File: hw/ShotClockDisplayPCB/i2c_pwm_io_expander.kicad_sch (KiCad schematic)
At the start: 0 parts

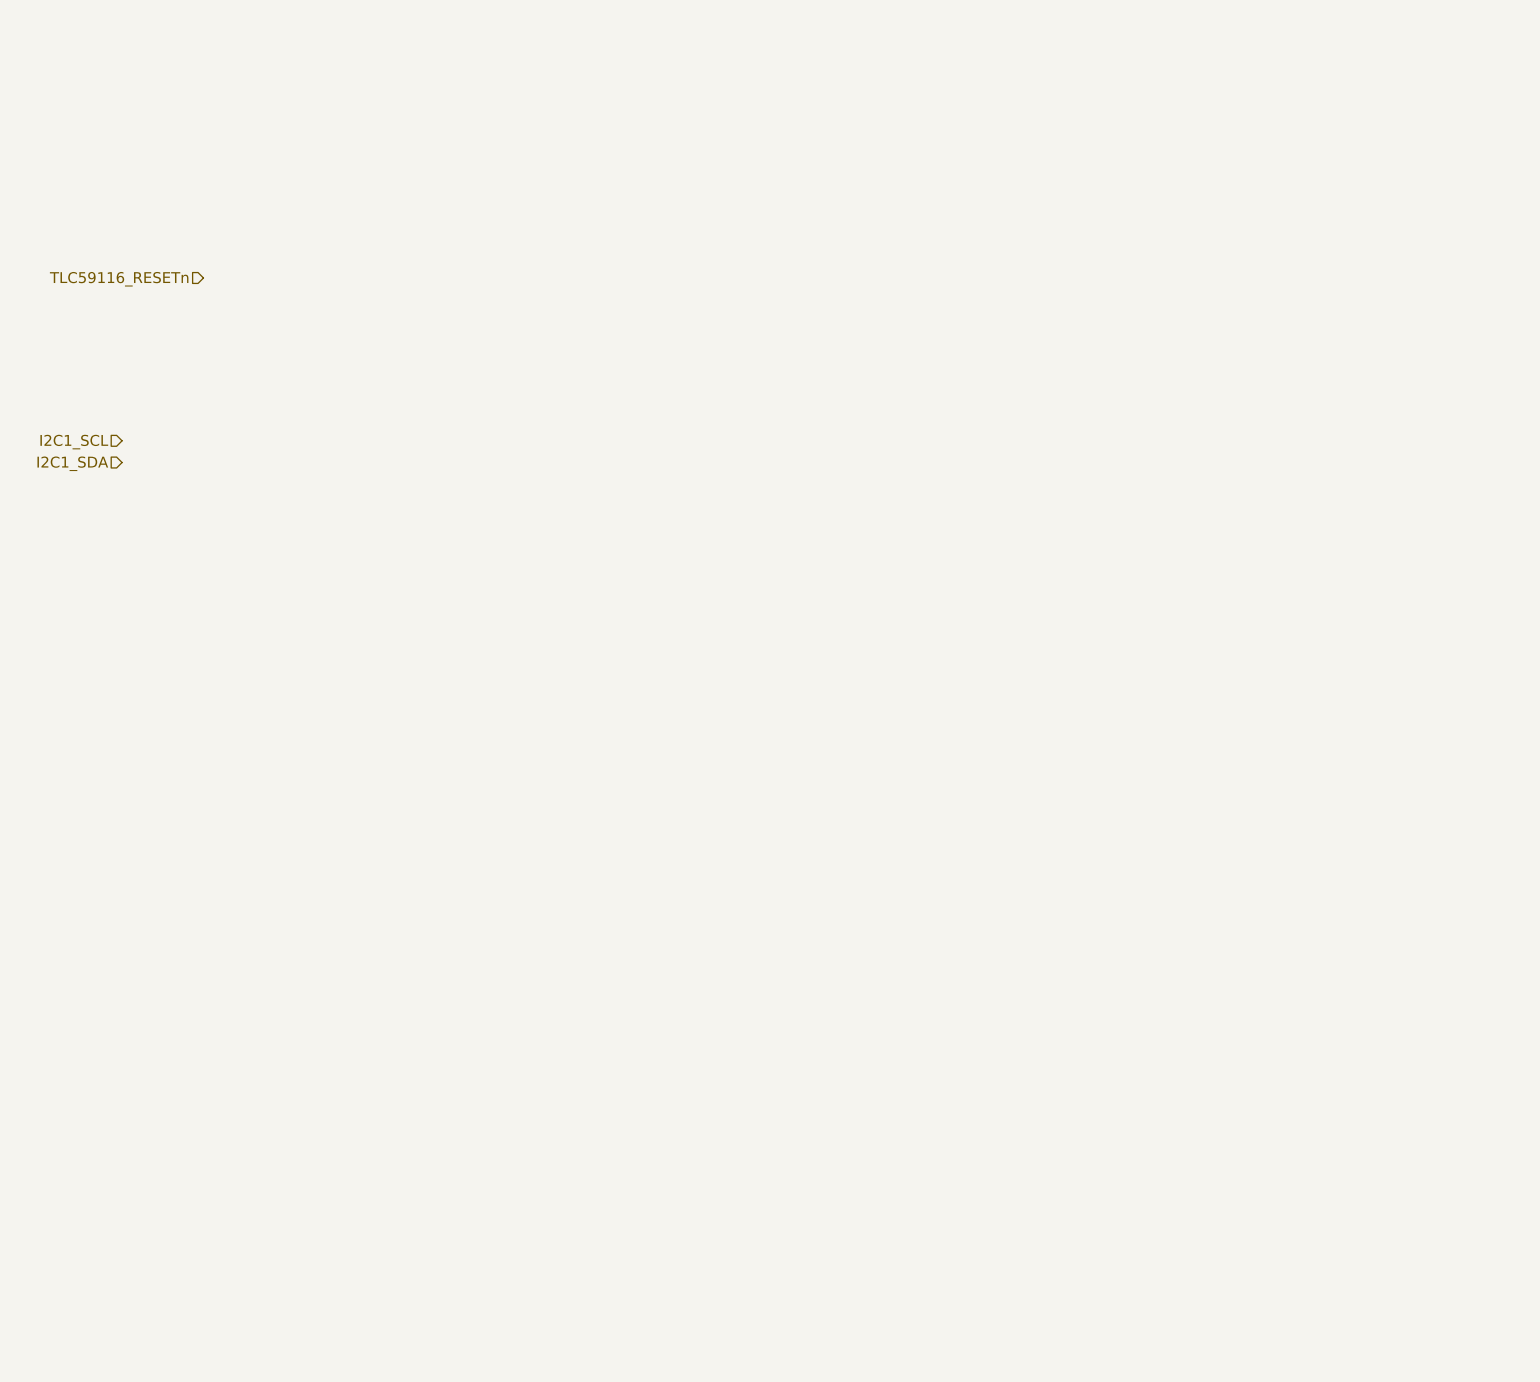
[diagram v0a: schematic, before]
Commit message: Started on display board rework
added new footprints
added HW select shunts/jumpers
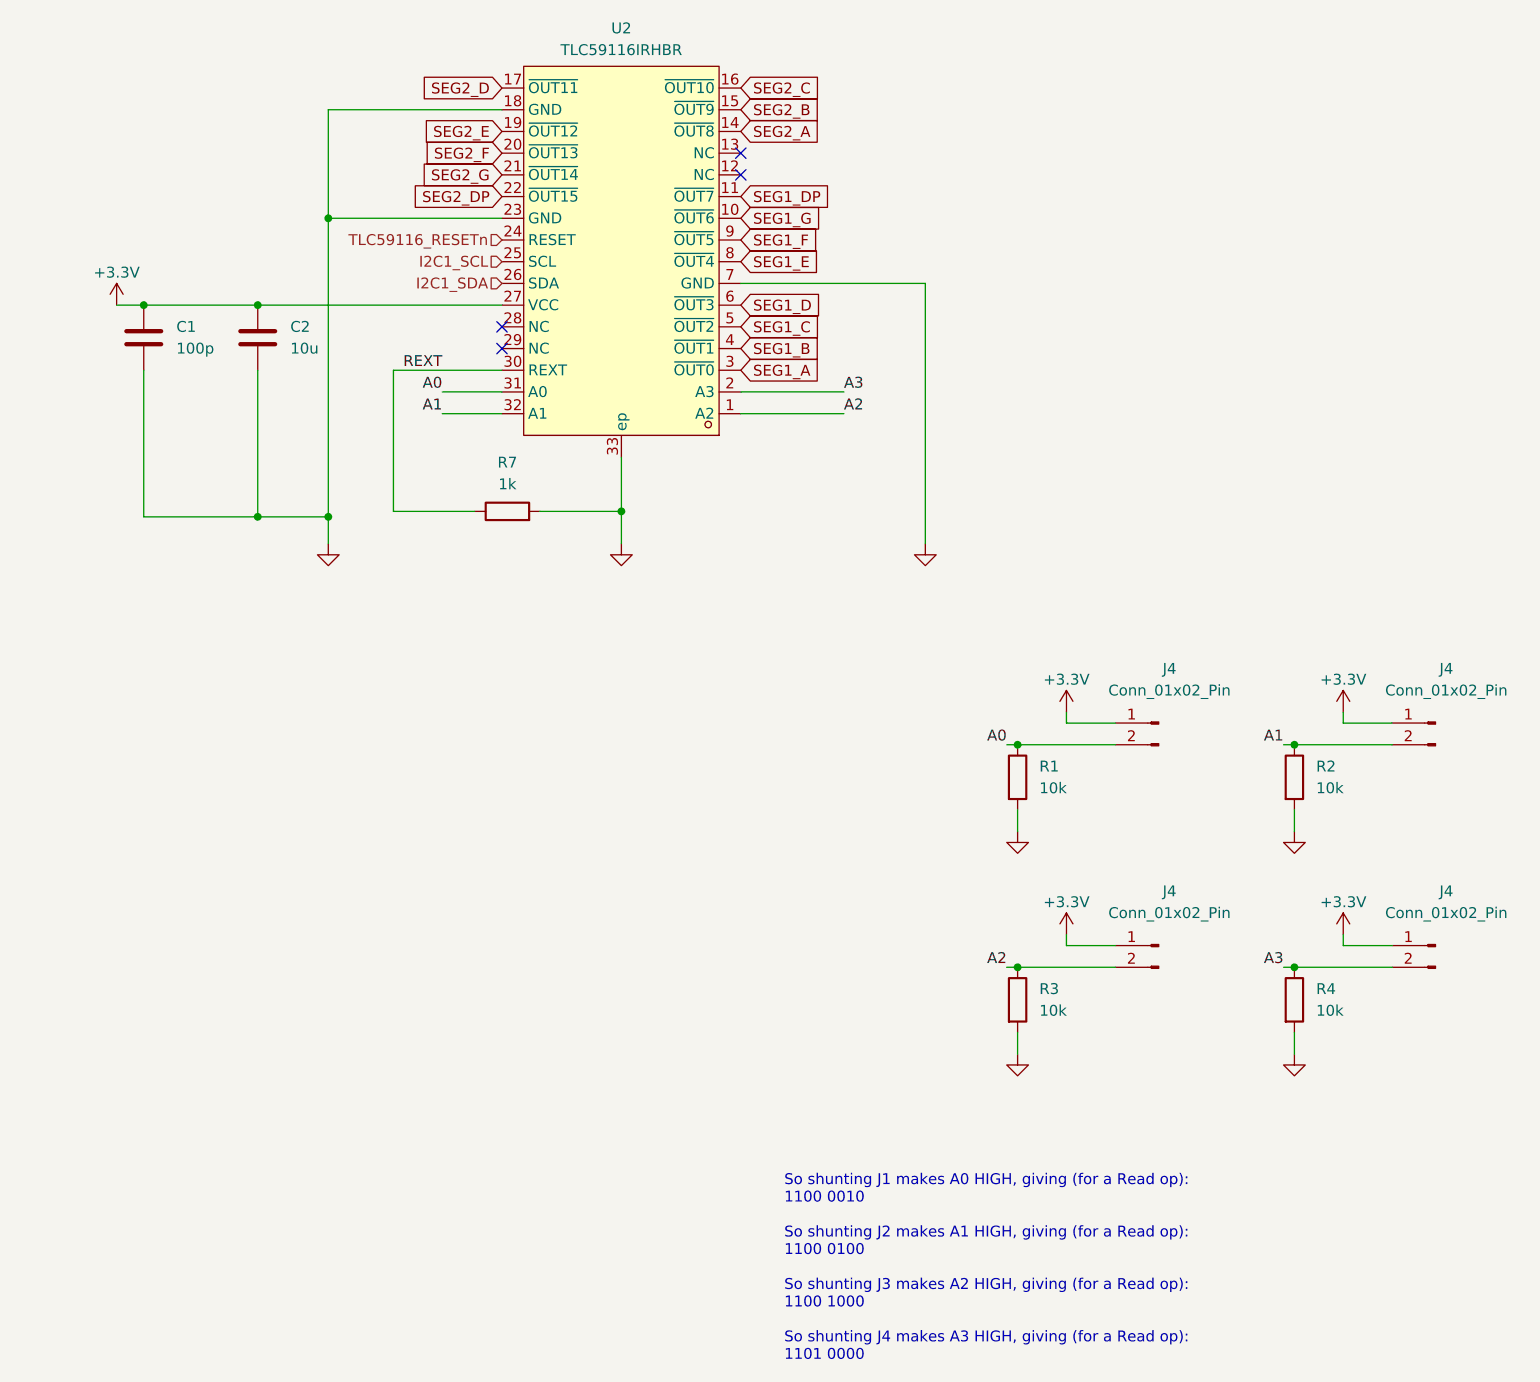
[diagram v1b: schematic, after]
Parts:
- added C1: 100p, Capacitor_SMD:C_0402_1005Metric, symbol Device:C
- added C2: 10u, Capacitor_SMD:C_0402_1005Metric, symbol Device:C
- added J4 (x4): Conn_01x02_Pin, Connector_PinHeader_2.54mm:PinHeader_1x02_P2.54mm_Horizontal, symbol Connector:Conn_01x02_Pin
- added R1, R2, R3, R4: 10k, Resistor_SMD:R_0402_1005Metric, symbol Device:R
- added R7: 1k, Resistor_SMD:R_0402_1005Metric, symbol Device:R
- added U2: TLC59116IRHBR, TLC59116IRHBR:PG-VQFN-32_L5.0-W5.0-P0.50-BL-EP3.6, symbol TLC59116IRHBR:TLC59116IRHBR
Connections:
- net I2C1_SCL: now also U2.25 (SCL)
- net I2C1_SDA: now also U2.26 (SDA)
- net TLC59116_RESETn: now also U2.24 (RESET)
- new net +3.3V: C1.1, C2.1, J4.1 (Pin_1), J4.1 (Pin_1), J4.1 (Pin_1), J4.1 (Pin_1), U2.27 (VCC)
- new net A0: J4.2 (Pin_2), R1.1, U2.31 (A0)
- new net A1: J4.2 (Pin_2), R2.1, U2.32 (A1)
- new net A2: J4.2 (Pin_2), R3.1, U2.1 (A2)
- new net A3: J4.2 (Pin_2), R4.1, U2.2 (A3)
- new net GND: C1.2, C2.2, R1.2, R2.2, R3.2, R4.2, R7.2, U2.18 (GND), U2.23 (GND), U2.33 (ep), U2.7 (GND)
- new net REXT: R7.1, U2.30 (REXT)
- new net SEG1_A: U2.3 (~{OUT0})
- new net SEG1_B: U2.4 (~{OUT1})
- new net SEG1_C: U2.5 (~{OUT2})
- new net SEG1_D: U2.6 (~{OUT3})
- new net SEG1_DP: U2.11 (~{OUT7})
- new net SEG1_E: U2.8 (~{OUT4})
- new net SEG1_F: U2.9 (~{OUT5})
- new net SEG1_G: U2.10 (~{OUT6})
- new net SEG2_A: U2.14 (~{OUT8})
- new net SEG2_B: U2.15 (~{OUT9})
- new net SEG2_C: U2.16 (~{OUT10})
- new net SEG2_D: U2.17 (~{OUT11})
- new net SEG2_DP: U2.22 (~{OUT15})
- new net SEG2_E: U2.19 (~{OUT12})
- new net SEG2_F: U2.20 (~{OUT13})
- new net SEG2_G: U2.21 (~{OUT14})
- no-connect marks 0 -> 4
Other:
- note added: "So shunting J1 makes A0 HIGH, giving (for a Read op): 1100 0010 So shunting J2 makes A1 HIGH, giving (for a Read op): 1100 0100 So shunting J3 makes A2 HIGH, giving (for a Read op): 1100 1000 So shunting J4 makes A3 HIGH, giving (for a Read op): 1101 0000"

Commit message: Changed LCSC Part numbers for disp board
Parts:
- C1: LCSC Part (none) -> C106200
- C2: LCSC Part (none) -> C315248
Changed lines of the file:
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@@
+      (effects (font (size 1.27 1.27)) hide)
+    )
+    (property "LCSC Part" "C315248" (at 47.625 64.135 0)
       (effects (font (size 1.27 1.27)) hide)
     )
@@
       (effects (font (size 1.27 1.27)) hide)
     )
+    (property "LCSC Part" "C106200" (at 34.29 64.135 0)
+      (effects (font (size 1.27 1.27)) hide)
+    )

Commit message: REV2 Finished
Corrected LCSC part number
Added polarities on silkscreen
Made output files for both boards
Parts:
- J4: LCSC Part C225269 -> C492410
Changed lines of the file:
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@@
       (effects (font (size 1.27 1.27)) hide)
     )
-    (property "LCSC Part #" "" (at 185.42 109.22 0)
-      (effects (font (size 1.27 1.27)) hide)
-    )
-    (property "LCSC Part" "C225269" (at 185.42 109.22 0)
+    (property "LCSC Part" "C492410" (at 185.42 109.22 0)
       (effects (font (size 1.27 1.27)) hide)
     )
@@
       (effects (font (size 1.27 1.27)) hide)
     )
-    (property "LCSC Part #" "" (at 185.42 135.255 0)
-      (effects (font (size 1.27 1.27)) hide)
-    )
-    (property "LCSC Part" "C225269" (at 185.42 135.255 0)
+    (property "LCSC Part" "C492410" (at 185.42 135.255 0)
       (effects (font (size 1.27 1.27)) hide)
     )
@@
       (effects (font (size 1.27 1.27)) hide)
     )
-    (property "LCSC Part #" "" (at 153.035 109.22 0)
-      (effects (font (size 1.27 1.27)) hide)
-    )
-    (property "LCSC Part" "C225269" (at 153.035 109.22 0)
+    (property "LCSC Part" "C492410" (at 153.035 109.22 0)
       (effects (font (size 1.27 1.27)) hide)
     )
@@
       (effects (font (size 1.27 1.27)) hide)
     )
-    (property "LCSC Part #" "" (at 153.035 135.255 0)
-      (effects (font (size 1.27 1.27)) hide)
-    )
-    (property "LCSC Part" "C225269" (at 153.035 135.255 0)
-      (effects (font (size 1.27 1.27)) hide)
-    )
+    (property "LCSC Part" "C492410" (at 153.035 135.255 0)
+      (effects (font (size 1.27 1.27)) hide)
+    )
